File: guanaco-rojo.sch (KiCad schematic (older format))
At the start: 21 parts, among them J1 Conn_01x02, J2 Input, J3 Output, U1 4049

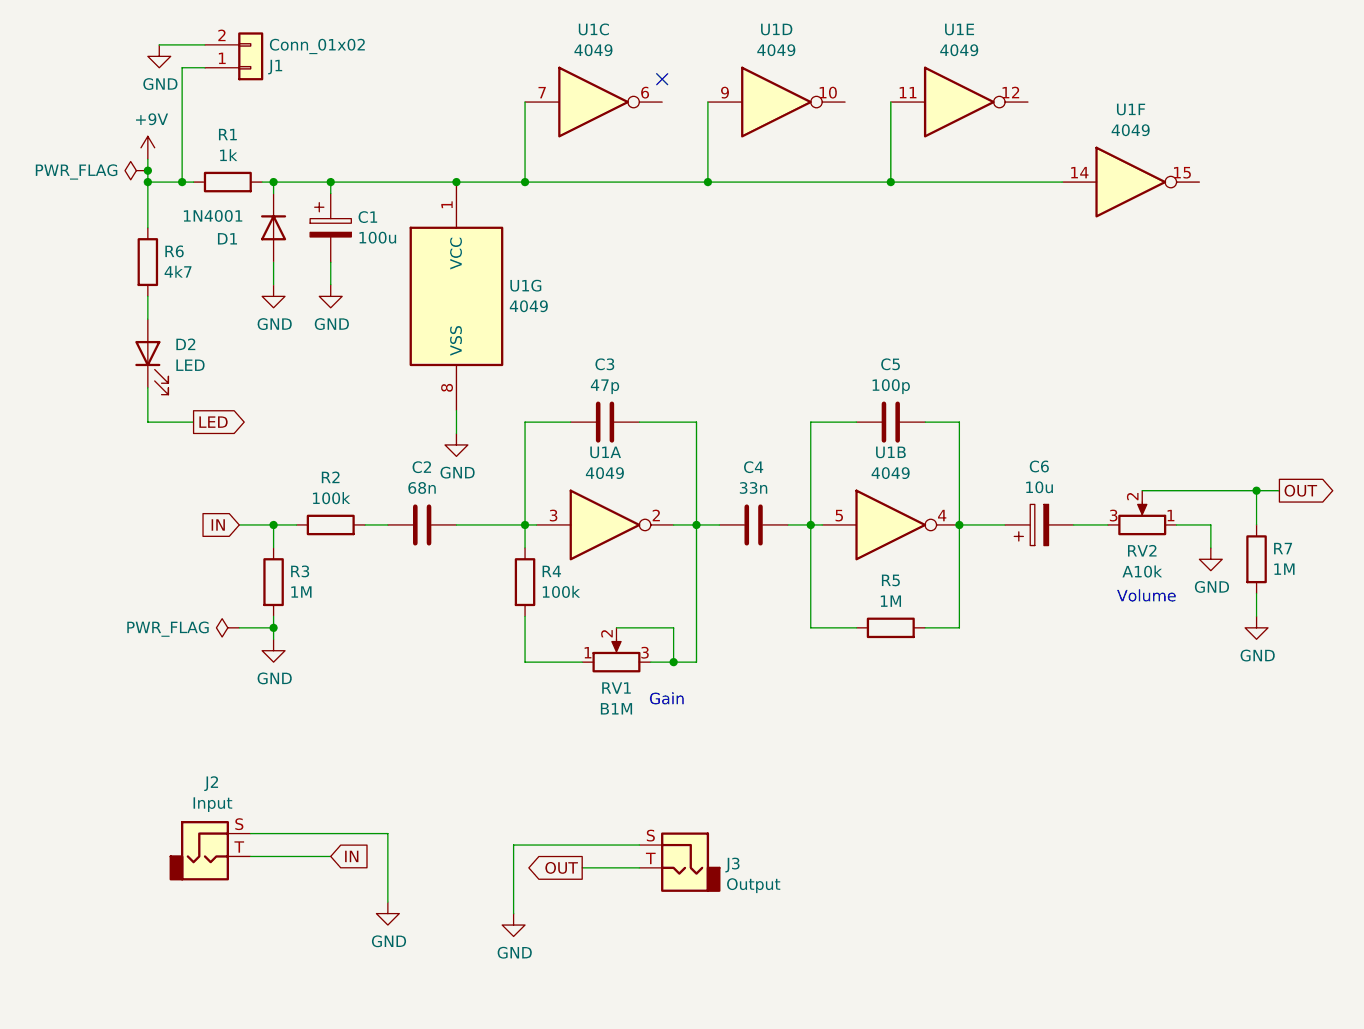
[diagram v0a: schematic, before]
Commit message: v0.2: pcb rerouted for 9 mm pots, unverified
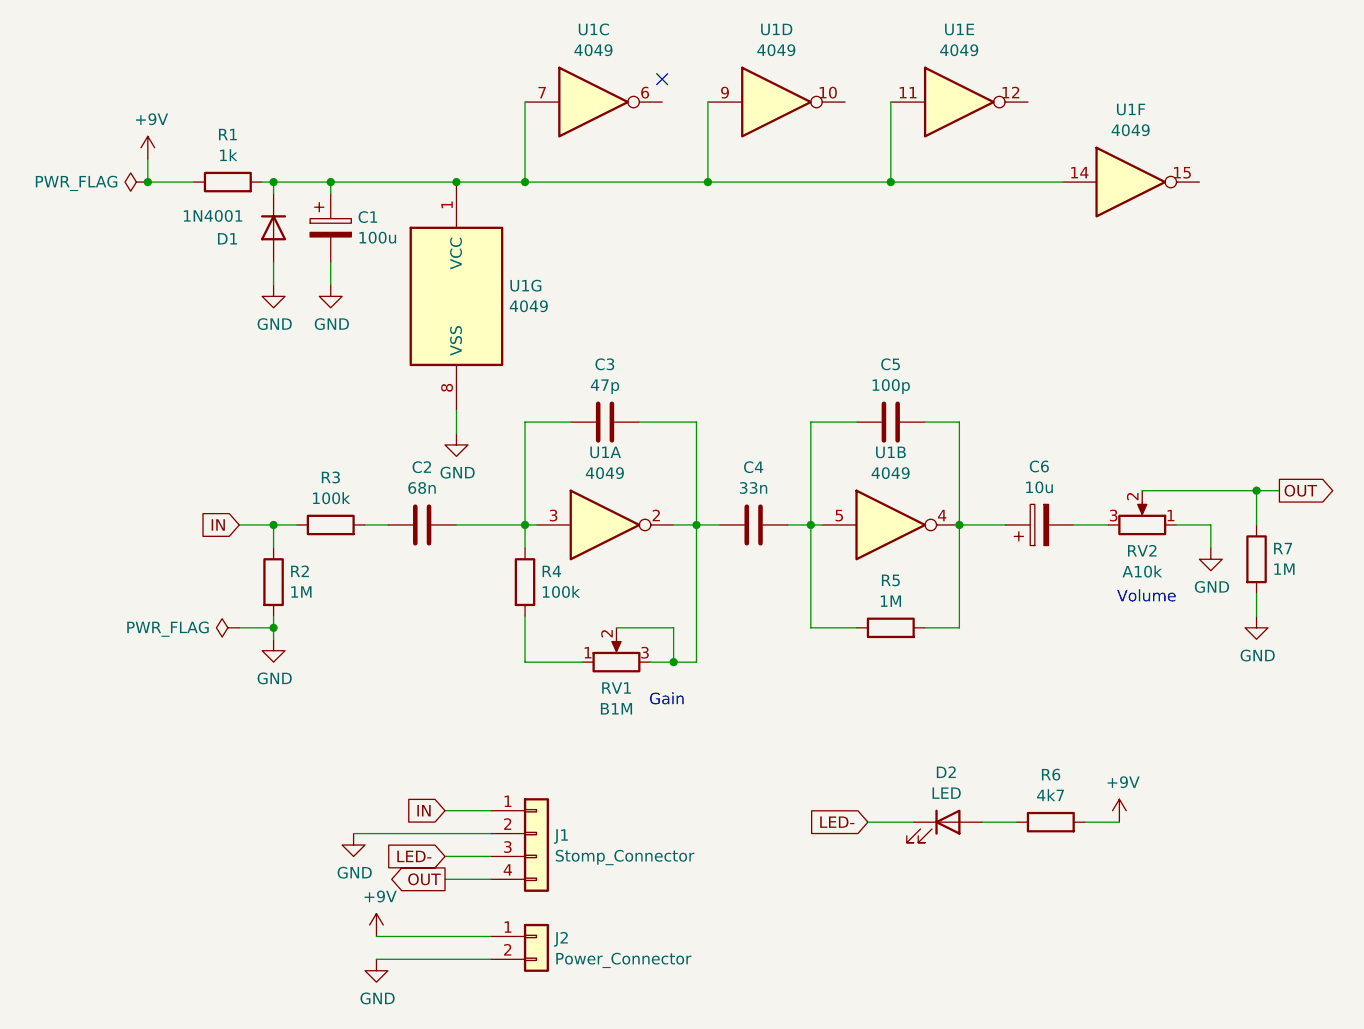
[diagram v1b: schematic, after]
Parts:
- removed J1: Conn_01x02, Connector_PinHeader_2.54mm:PinHeader_1x02_P2.54mm_Vertical, symbol Connector_Generic:Conn_01x02
- removed J2: Input, Connector_PinHeader_2.54mm:PinHeader_1x02_P2.54mm_Vertical, symbol Connector:AudioJack2
- removed J3: Output, Connector_PinHeader_2.54mm:PinHeader_1x02_P2.54mm_Vertical, symbol Connector:AudioJack2
- added J1: Stomp_Connector, rockola_kicad_footprints:Stomp_4pin, symbol rockola_kicad_symbols:Stomp_Connector
- added J2: Power_Connector, rockola_kicad_footprints:Power_Header_2pin, symbol rockola_kicad_symbols:Power_Connector
- D2: footprint OPL_Connector:H2-2.54 -> LED_THT:LED_D5.0mm
- RV1, RV2: footprint OPL_Connector:H3-2.54 -> potentiometers:9MM_METAL_SHAFT
- renumbered R3 to R2, R2 to R3
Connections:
- net +9V: now also R6.2, J2.1 (PWR); no longer R6.1
- net GND: now also J1.2 (GND), J2.2 (GND)
- net IN: now also J1.1 (IN)
- net OUT: now also J1.4 (OUT)
- net at D2.2 (A): now also R6.1; no longer R6.2
- net LED renamed LED-
- net LED-: now also J1.3 (SW)
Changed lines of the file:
@@
 EESchema Schematic File Version 5
-EELAYER 31 0
+EELAYER 32 0
 EELAYER END
 $Descr A4 11693 8268
@@
 Comment9 ""
 $EndDescr
-Connection ~ 1400 1700
+Connection ~ 3800 3250
+Connection ~ 2200 1750
+Connection ~ 6250 3100
+Connection ~ 1950 1750
+Connection ~ 3850 1750
+Connection ~ 3050 1750
+Connection ~ 4950 3250
+Connection ~ 3050 3250
+Connection ~ 1950 3250
+Connection ~ 3700 3850
+Connection ~ 2750 1750
+Connection ~ 1950 3700
+Connection ~ 4650 1750
+Connection ~ 4300 3250
 Connection ~ 1400 1750
-Connection ~ 1550 1750
-Connection ~ 1950 1750
-Connection ~ 1950 3250
-Connection ~ 1950 3700
-Connection ~ 2200 1750
-Connection ~ 2750 1750
-Connection ~ 3050 1750
-Connection ~ 3050 3250
-Connection ~ 3700 3850
-Connection ~ 3800 3250
-Connection ~ 3850 1750
-Connection ~ 4300 3250
-Connection ~ 4650 1750
-Connection ~ 4950 3250
-Connection ~ 6250 3100
 NoConn ~ 3650 1300
 Wire Wire Line
-	1400 1650 1400 1700
-Wire Wire Line
-	1400 1700 1400 1750
-Wire Wire Line
-	1400 1750 1400 1950
-Wire Wire Line
-	1400 1750 1550 1750
-Wire Wire Line
-	1400 2250 1400 2350
-Wire Wire Line
-	1400 2800 1400 2650
-Wire Wire Line
-	1450 1150 1650 1150
-Wire Wire Line
-	1550 1250 1550 1750
-Wire Wire Line
-	1550 1750 1600 1750
-Wire Wire Line
-	1600 2800 1400 2800
-Wire Wire Line
-	1650 1250 1550 1250
+	1400 1650 1400 1750
+Wire Wire Line
+	1400 1750 1600 1750
 Wire Wire Line
 	1800 3250 1950 3250
@@
 	1800 3700 1950 3700
 Wire Wire Line
-	1850 4700 2200 4700
-Wire Wire Line
 	1950 1750 1900 1750
 Wire Wire Line
@@
 	2200 2100 2200 2200
 Wire Wire Line
+	2300 4600 2900 4600
+Wire Wire Line
 	2350 3250 2450 3250
 Wire Wire Line
-	2450 4600 1850 4600
-Wire Wire Line
-	2450 4900 2450 4600
+	2400 5050 2900 5050
+Wire Wire Line
+	2400 5150 2900 5150
+Wire Wire Line
+	2700 4500 2900 4500
+Wire Wire Line
+	2700 4700 2900 4700
+Wire Wire Line
+	2700 4800 2900 4800
 Wire Wire Line
 	2750 1750 3050 1750
@@
 	2750 3250 3050 3250
 Wire Wire Line
-	3000 4650 3000 4950
-Wire Wire Line
 	3050 1400 3050 1750
 Wire Wire Line
@@
 	3250 2800 3050 2800
 Wire Wire Line
-	3300 4750 3550 4750
-Wire Wire Line
 	3450 3700 3700 3700
 Wire Wire Line
 	3550 2800 3800 2800
 Wire Wire Line
-	3550 4650 3000 4650
-Wire Wire Line
 	3600 3850 3700 3850
 Wire Wire Line
@@
 	4500 3700 4300 3700
 Wire Wire Line
+	4550 4550 4750 4550
+Wire Wire Line
 	4650 1400 4650 1750
 Wire Wire Line
@@
 	4950 3700 4800 3700
 Wire Wire Line
+	5050 4550 5200 4550
+Wire Wire Line
 	5450 3250 5600 3250
+Wire Wire Line
+	5500 4550 5650 4550
 Wire Wire Line
 	5750 3100 6250 3100
@@
 Text Notes 5900 3600 2    50   ~ 0
 Volume\n
-Text GLabel 1600 2800 2    50   Output ~ 0
-LED
 Text GLabel 1800 3250 0    50   Input ~ 0
 IN
-Text GLabel 2200 4700 2    50   Input ~ 0
+Text GLabel 2700 4500 0    50   Input ~ 0
 IN
-Text GLabel 3300 4750 0    50   Output ~ 0
+Text GLabel 2700 4700 0    50   Input ~ 0
+LED-
+Text GLabel 2700 4800 0    50   Output ~ 0
 OUT
+Text GLabel 4550 4550 0    50   Input ~ 0
+LED-
 Text GLabel 6350 3100 2    50   Output ~ 0
 OUT
@@
 L power:PWR_FLAG #FLG01
 U 1 1 5E4FAADC
-P 1400 1700
-F 0 "#FLG01" H 1400 1775 50  0001 C CNN
-F 1 "PWR_FLAG" V 1400 1828 50  0000 L CNN
-F 2 "" H 1400 1700 50  0001 C CNN
-F 3 "~" H 1400 1700 50  0001 C CNN
-	1    1400 1700
+P 1400 1750
+F 0 "#FLG01" H 1400 1825 50  0001 C CNN
+F 1 "PWR_FLAG" V 1400 1878 50  0000 L CNN
+F 2 "" H 1400 1750 50  0001 C CNN
+F 3 "~" H 1400 1750 50  0001 C CNN
+	1    1400 1750
 	0    -1   -1   0
 $EndComp
@@
 $EndComp
 $Comp
-L power:GND #PWR08
-U 1 1 5E5871BF
-P 1450 1150
-F 0 "#PWR08" H 1450 900 50  0001 C CNN
-F 1 "GND" H 1455 977 50  0000 C CNN
-F 2 "" H 1450 1150 50  0001 C CNN
-F 3 "" H 1450 1150 50  0001 C CNN
-	1    1450 1150
+L power:+9V #PWR06
+U 1 1 5E743817
+P 2400 5050
+F 0 "#PWR06" H 2400 4900 50  0001 C CNN
+F 1 "+9V" H 2415 5223 50  0000 C CNN
+F 2 "" H 2400 5050 50  0001 C CNN
+F 3 "" H 2400 5050 50  0001 C CNN
+	1    2400 5050
+	1    0    0    -1
+$EndComp
+$Comp
+L power:+9V #PWR09
+U 1 1 5E72E2EA
+P 5650 4550
+F 0 "#PWR09" H 5650 4400 50  0001 C CNN
+F 1 "+9V" H 5665 4723 50  0000 C CNN
+F 2 "" H 5650 4550 50  0001 C CNN
+F 3 "" H 5650 4550 50  0001 C CNN
+	1    5650 4550
 	1    0    0    -1
 $EndComp
@@
 $EndComp
 $Comp
-L power:GND #PWR09
-U 1 1 5E58AAF2
-P 2450 4900
-F 0 "#PWR09" H 2450 4650 50  0001 C CNN
-F 1 "GND" H 2455 4727 50  0000 C CNN
-F 2 "" H 2450 4900 50  0001 C CNN
-F 3 "" H 2450 4900 50  0001 C CNN
-	1    2450 4900
-	1    0    0    -1
-$EndComp
-$Comp
 L power:GND #PWR05
+U 1 1 5E7250A2
+P 2300 4600
+F 0 "#PWR05" H 2300 4350 50  0001 C CNN
+F 1 "GND" H 2305 4427 50  0000 C CNN
+F 2 "" H 2300 4600 50  0001 C CNN
+F 3 "" H 2300 4600 50  0001 C CNN
+	1    2300 4600
+	1    0    0    -1
+$EndComp
+$Comp
+L power:GND #PWR07
+U 1 1 5E743D60
+P 2400 5150
+F 0 "#PWR07" H 2400 4900 50  0001 C CNN
+F 1 "GND" H 2405 4977 50  0000 C CNN
+F 2 "" H 2400 5150 50  0001 C CNN
+F 3 "" H 2400 5150 50  0001 C CNN
+	1    2400 5150
+	1    0    0    -1
+$EndComp
+$Comp
+L power:GND #PWR08
 U 1 1 5E521728
 P 2750 2850
-F 0 "#PWR05" H 2750 2600 50  0001 C CNN
+F 0 "#PWR08" H 2750 2600 50  0001 C CNN
 F 1 "GND" H 2755 2677 50  0000 C CNN
 F 2 "" H 2750 2850 50  0001 C CNN
@@
 $Comp
 L power:GND #PWR010
-U 1 1 5E591B5E
-P 3000 4950
-F 0 "#PWR010" H 3000 4700 50  0001 C CNN
-F 1 "GND" H 3005 4777 50  0000 C CNN
-F 2 "" H 3000 4950 50  0001 C CNN
-F 3 "" H 3000 4950 50  0001 C CNN
-	1    3000 4950
-	1    0    0    -1
-$EndComp
-$Comp
-L power:GND #PWR06
 U 1 1 5E55587C
 P 6050 3350
-F 0 "#PWR06" H 6050 3100 50  0001 C CNN
+F 0 "#PWR010" H 6050 3100 50  0001 C CNN
 F 1 "GND" H 6055 3177 50  0000 C CNN
 F 2 "" H 6050 3350 50  0001 C CNN
@@
 $EndComp
 $Comp
-L power:GND #PWR07
+L power:GND #PWR011
 U 1 1 5E567FF7
 P 6250 3650
-F 0 "#PWR07" H 6250 3400 50  0001 C CNN
+F 0 "#PWR011" H 6250 3400 50  0001 C CNN
 F 1 "GND" H 6255 3477 50  0000 C CNN
 F 2 "" H 6250 3650 50  0001 C CNN
 F 3 "" H 6250 3650 50  0001 C CNN
 	1    6250 3650
-	1    0    0    -1
-$EndComp
-$Comp
-L Device:R R6
-U 1 1 5E55A984
-P 1400 2100
-F 0 "R6" H 1470 2145 50  0000 L CNN
-F 1 "4k7" H 1470 2055 50  0000 L CNN
-F 2 "Resistor_THT:R_Axial_DIN0207_L6.3mm_D2.5mm_P7.62mm_Horizontal" V 1330 2100 50  0001 C CNN
-F 3 "~" H 1400 2100 50  0001 C CNN
-	1    1400 2100
 	1    0    0    -1
 $EndComp
@@
 $EndComp
 $Comp
-L Device:R R3
+L Device:R R2
 U 1 1 5E5438CE
 P 1950 3500
-F 0 "R3" H 2020 3545 50  0000 L CNN
+F 0 "R2" H 2020 3545 50  0000 L CNN
 F 1 "1M" H 2020 3455 50  0000 L CNN
 F 2 "Resistor_THT:R_Axial_DIN0207_L6.3mm_D2.5mm_P7.62mm_Horizontal" V 1880 3500 50  0001 C CNN
@@
 $EndComp
 $Comp
-L Device:R R2
+L Device:R R3
 U 1 1 5E548EBB
 P 2200 3250
-F 0 "R2" V 2406 3250 50  0000 C CNN
+F 0 "R3" V 2406 3250 50  0000 C CNN
 F 1 "100k" V 2315 3250 50  0000 C CNN
 F 2 "Resistor_THT:R_Axial_DIN0207_L6.3mm_D2.5mm_P7.62mm_Horizontal" V 2130 3250 50  0001 C CNN
@@
 F 3 "~" H 4650 3700 50  0001 C CNN
 	1    4650 3700
+	0    -1   -1   0
+$EndComp
+$Comp
+L Device:R R6
+U 1 1 5E72BEDF
+P 5350 4550
+F 0 "R6" V 5556 4550 50  0000 C CNN
+F 1 "4k7" V 5465 4550 50  0000 C CNN
+F 2 "Resistor_THT:R_Axial_DIN0207_L6.3mm_D2.5mm_P7.62mm_Horizontal" V 5280 4550 50  0001 C CNN
+F 3 "~" H 5350 4550 50  0001 C CNN
+	1    5350 4550
 	0    -1   -1   0
 $EndComp
@@
 $Comp
 L Device:LED D2
-U 1 1 5E55B5B8
-P 1400 2500
-F 0 "D2" V 1438 2382 50  0000 R CNN
-F 1 "LED" V 1347 2382 50  0000 R CNN
-F 2 "OPL_Connector:H2-2.54" H 1400 2500 50  0001 C CNN
-F 3 "~" H 1400 2500 50  0001 C CNN
-	1    1400 2500
-	0    -1   -1   0
-$EndComp
-$Comp
-L Connector_Generic:Conn_01x02 J1
-U 1 1 5E57A721
-P 1850 1250
-F 0 "J1" H 1930 1242 50  0000 L CNN
-F 1 "Conn_01x02" H 1930 1151 50  0000 L CNN
-F 2 "Connector_PinHeader_2.54mm:PinHeader_1x02_P2.54mm_Vertical" H 1850 1250 50  0001 C CNN
-F 3 "~" H 1850 1250 50  0001 C CNN
-	1    1850 1250
-	1    0    0    1
+U 1 1 5E729700
+P 4900 4550
+F 0 "D2" H 4893 4766 50  0000 C CNN
+F 1 "LED" H 4893 4675 50  0000 C CNN
+F 2 "LED_THT:LED_D5.0mm" H 4900 4550 50  0001 C CNN
+F 3 "~" H 4900 4550 50  0001 C CNN
+	1    4900 4550
+	1    0    0    -1
+$EndComp
+$Comp
+L rockola_kicad_symbols:Power_Connector J2
+U 1 1 5E73BB6D
+P 3100 5050
+F 0 "J2" H 3180 5042 50  0000 L CNN
+F 1 "Power_Connector" H 3180 4951 50  0000 L CNN
+F 2 "rockola_kicad_footprints:Power_Header_2pin" H 3100 5050 50  0001 C CNN
+F 3 "~" H 3100 5050 50  0001 C CNN
+	1    3100 5050
+	1    0    0    -1
 $EndComp
 $Comp
@@
 F 0 "RV1" V 3335 3850 50  0000 C CNN
 F 1 "B1M" V 3244 3850 50  0000 C CNN
-F 2 "OPL_Connector:H3-2.54" H 3450 3850 50  0001 C CNN
+F 2 "potentiometers:9MM_METAL_SHAFT" H 3450 3850 50  0001 C CNN
 F 3 "~" H 3450 3850 50  0001 C CNN
 	1    3450 3850
@@
 F 0 "RV2" V 5635 3250 50  0000 C CNN
 F 1 "A10k" V 5544 3250 50  0000 C CNN
-F 2 "OPL_Connector:H3-2.54" H 5750 3250 50  0001 C CNN
+F 2 "potentiometers:9MM_METAL_SHAFT" H 5750 3250 50  0001 C CNN
 F 3 "~" H 5750 3250 50  0001 C CNN
 	1    5750 3250
@@
 $EndComp
 $Comp
-L Connector:AudioJack2 J2
-U 1 1 5E588642
-P 1650 4700
-F 0 "J2" H 1682 5023 50  0000 C CNN
-F 1 "Input" H 1682 4932 50  0000 C CNN
-F 2 "Connector_PinHeader_2.54mm:PinHeader_1x02_P2.54mm_Vertical" H 1650 4700 50  0001 C CNN
-F 3 "~" H 1650 4700 50  0001 C CNN
-	1    1650 4700
-	1    0    0    -1
-$EndComp
-$Comp
-L Connector:AudioJack2 J3
-U 1 1 5E58B6A5
-P 3750 4750
-F 0 "J3" H 3570 4767 50  0000 R CNN
-F 1 "Output" H 3570 4677 50  0000 R CNN
-F 2 "Connector_PinHeader_2.54mm:PinHeader_1x02_P2.54mm_Vertical" H 3750 4750 50  0001 C CNN
-F 3 "~" H 3750 4750 50  0001 C CNN
-	1    3750 4750
-	-1   0    0    -1
-$EndComp
-$Comp
+L rockola_kicad_symbols:Stomp_Connector J1
+U 1 1 5E7170D8
+P 3100 4600
+F 0 "J1" H 3180 4592 50  0000 L CNN
+F 1 "Stomp_Connector" H 3180 4501 50  0000 L CNN
+F 2 "rockola_kicad_footprints:Stomp_4pin" H 3100 4600 50  0001 C CNN
+F 3 "~" H 3100 4600 50  0001 C CNN
+	1    3100 4600
+	1    0    0    -1
+$EndComp
+$Comp

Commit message: real v0.3 files
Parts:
- added J3: Alt. power, rockola_kicad_footprints:Power_Header_2pin, symbol rockola_kicad_symbols:Power_Connector
- J2: footprint rockola_kicad_footprints:Power_Header_2pin -> rockola_kicad_footprints:Power_Header_2pin_TOP
- U1: footprint Package_DIP:DIP-16_W7.62mm -> Package_SO:SOIC-16_3.9x9.9mm_P1.27mm
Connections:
- net +9V: now also J3.1 (PWR)
- net GND: now also J3.2 (GND)
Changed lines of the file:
@@
+$EndComp
+$Comp
+L power:+9V #PWR012
+U 1 1 5E74ABE8
+P 5000 5050
+F 0 "#PWR012" H 5000 4900 50  0001 C CNN
+F 1 "+9V" H 5015 5223 50  0000 C CNN
+F 2 "" H 5000 5050 50  0001 C CNN
+F 3 "" H 5000 5050 50  0001 C CNN
+	1    5000 5050
+	1    0    0    -1
 $EndComp
 $Comp
@@
 F 3 "" H 2750 2850 50  0001 C CNN
 	1    2750 2850
+	1    0    0    -1
+$EndComp
+$Comp
+L power:GND #PWR013
+U 1 1 5E74C04C
+P 5000 5150
+F 0 "#PWR013" H 5000 4900 50  0001 C CNN
+F 1 "GND" H 5005 4977 50  0000 C CNN
+F 2 "" H 5000 5150 50  0001 C CNN
+F 3 "" H 5000 5150 50  0001 C CNN
+	1    5000 5150
 	1    0    0    -1
 $EndComp
@@
 F 0 "J2" H 3180 5042 50  0000 L CNN
 F 1 "Power_Connector" H 3180 4951 50  0000 L CNN
-F 2 "rockola_kicad_footprints:Power_Header_2pin" H 3100 5050 50  0001 C CNN
+F 2 "rockola_kicad_footprints:Power_Header_2pin_TOP" H 3100 5050 50  0001 C CNN
 F 3 "~" H 3100 5050 50  0001 C CNN
 	1    3100 5050
+	1    0    0    -1
+$EndComp
+$Comp
+L rockola_kicad_symbols:Power_Connector J3
+U 1 1 5E7427D2
+P 5200 5050
+F 0 "J3" H 5280 5042 50  0000 L CNN
+F 1 "Alt. power" H 5280 4951 50  0000 L CNN
+F 2 "rockola_kicad_footprints:Power_Header_2pin" H 5200 5050 50  0001 C CNN
+F 3 "~" H 5200 5050 50  0001 C CNN
+	1    5200 5050
 	1    0    0    -1
 $EndComp
@@
 F 0 "U1" H 3350 1716 50  0000 C CNN
 F 1 "4049" H 3350 1625 50  0000 C CNN
-F 2 "Package_DIP:DIP-16_W7.62mm" H 3350 1400 50  0001 C CNN
+F 2 "Package_SO:SOIC-16_3.9x9.9mm_P1.27mm" H 3350 1400 50  0001 C CNN
 F 3 "http://www.intersil.com/content/dam/intersil/documents/cd40/cd4049ubms.pdf" H 3350 1400 50  0001 C CNN
 	3    3350 1400
@@
 F 0 "U1" H 3400 3566 50  0000 C CNN
 F 1 "4049" H 3400 3475 50  0000 C CNN
-F 2 "Package_DIP:DIP-16_W7.62mm" H 3400 3250 50  0001 C CNN
+F 2 "Package_SO:SOIC-16_3.9x9.9mm_P1.27mm" H 3400 3250 50  0001 C CNN
 F 3 "http://www.intersil.com/content/dam/intersil/documents/cd40/cd4049ubms.pdf" H 3400 3250 50  0001 C CNN
 	1    3400 3250
@@
 F 0 "U1" H 4150 1716 50  0000 C CNN
 F 1 "4049" H 4150 1625 50  0000 C CNN
-F 2 "Package_DIP:DIP-16_W7.62mm" H 4150 1400 50  0001 C CNN
+F 2 "Package_SO:SOIC-16_3.9x9.9mm_P1.27mm" H 4150 1400 50  0001 C CNN
 F 3 "http://www.intersil.com/content/dam/intersil/documents/cd40/cd4049ubms.pdf" H 4150 1400 50  0001 C CNN
 	4    4150 1400
@@
 F 0 "U1" H 4650 3566 50  0000 C CNN
 F 1 "4049" H 4650 3475 50  0000 C CNN
-F 2 "Package_DIP:DIP-16_W7.62mm" H 4650 3250 50  0001 C CNN
+F 2 "Package_SO:SOIC-16_3.9x9.9mm_P1.27mm" H 4650 3250 50  0001 C CNN
 F 3 "http://www.intersil.com/content/dam/intersil/documents/cd40/cd4049ubms.pdf" H 4650 3250 50  0001 C CNN
 	2    4650 3250
@@
 F 0 "U1" H 4950 1716 50  0000 C CNN
 F 1 "4049" H 4950 1625 50  0000 C CNN
-F 2 "Package_DIP:DIP-16_W7.62mm" H 4950 1400 50  0001 C CNN
+F 2 "Package_SO:SOIC-16_3.9x9.9mm_P1.27mm" H 4950 1400 50  0001 C CNN
 F 3 "http://www.intersil.com/content/dam/intersil/documents/cd40/cd4049ubms.pdf" H 4950 1400 50  0001 C CNN
 	5    4950 1400
@@
 F 0 "U1" H 5700 2066 50  0000 C CNN
 F 1 "4049" H 5700 1975 50  0000 C CNN
-F 2 "Package_DIP:DIP-16_W7.62mm" H 5700 1750 50  0001 C CNN
+F 2 "Package_SO:SOIC-16_3.9x9.9mm_P1.27mm" H 5700 1750 50  0001 C CNN
 F 3 "http://www.intersil.com/content/dam/intersil/documents/cd40/cd4049ubms.pdf" H 5700 1750 50  0001 C CNN
 	6    5700 1750
@@
 F 0 "U1" H 2980 2295 50  0000 L CNN
 F 1 "4049" H 2980 2205 50  0000 L CNN
-F 2 "Package_DIP:DIP-16_W7.62mm" H 2750 2250 50  0001 C CNN
+F 2 "Package_SO:SOIC-16_3.9x9.9mm_P1.27mm" H 2750 2250 50  0001 C CNN
 F 3 "http://www.intersil.com/content/dam/intersil/documents/cd40/cd4049ubms.pdf" H 2750 2250 50  0001 C CNN
 	7    2750 2250
